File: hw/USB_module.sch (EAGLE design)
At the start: 34 parts, among them J1 GROVE-4P-2.0-3470130P1, J2 GROVE-4P-2.0-3470130P1, X1 22-23-2021, X2 47589-0001, X3 22-23-2021, X4 53047-04, X5 53047-04, X6 53047-06, X7 53047-06, X8 53047-06, X9 53047-04

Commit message: work in progress
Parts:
- U$6: value STM32F103CXTX -> STM32F303C; device st:STM32F103CXTX -> st:STM32F303C
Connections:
- removed net N$5: X7-5.S, X7-6.S
- removed net N$6: X8-5.S, X8-6.S
- net OSC_IN: now also U$6.PF0/OSC_IN; no longer U$6.PD0/OSC_IN
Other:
- moved on the sheet: X7-6, X8-6
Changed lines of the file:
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@@
 <part name="J1" library="OPL Eagle Library" deviceset="GROVE-4P-2.0" device="-3470130P1"/>
 <part name="+3V7" library="supply1" deviceset="+3V3" device=""/>
-<part name="U$6" library="st" deviceset="STM32F103CX" device="TX"/>
+<part name="U$6" library="st" deviceset="STM32F303C" device=""/>
 <part name="FRAME1" library="frames" deviceset="DINA3_L" device=""/>
 <part name="GND13" library="supply" deviceset="GND" device=""/>
@@
 <instance part="X7" gate="-4" x="254" y="139.7"/>
 <instance part="X7" gate="-5" x="254" y="137.16"/>
-<instance part="X7" gate="-6" x="254" y="137.16"/>
+<instance part="X7" gate="-6" x="254" y="134.62"/>
 <instance part="X8" gate="-1" x="254" y="124.46"/>
 <instance part="X8" gate="-2" x="254" y="121.92"/>
@@
 <instance part="X8" gate="-4" x="254" y="116.84"/>
 <instance part="X8" gate="-5" x="254" y="114.3"/>
-<instance part="X8" gate="-6" x="254" y="114.3"/>
+<instance part="X8" gate="-6" x="254" y="111.76"/>
 <instance part="X9" gate="-1" x="322.58" y="220.98"/>
 <instance part="X9" gate="-2" x="322.58" y="218.44"/>
@@
 <wire x1="50.8" y1="236.22" x2="50.8" y2="238.76" width="0.1524" layer="91"/>
 <label x="50.8" y="238.76" size="1.778" layer="95" rot="R90"/>
-<pinref part="U$6" gate="G$1" pin="PD0/OSC_IN"/>
+<pinref part="U$6" gate="G$1" pin="PF0/OSC_IN"/>
 </segment>
 <segment>
@@
 </segment>
 </net>
-<net name="N$5" class="0">
-<segment>
-<pinref part="X7" gate="-5" pin="S"/>
-<pinref part="X7" gate="-6" pin="S"/>
-</segment>
-</net>
-<net name="N$6" class="0">
-<segment>
-<pinref part="X8" gate="-5" pin="S"/>
-<pinref part="X8" gate="-6" pin="S"/>
-</segment>
-</net>

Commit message: layout of power oring section ongoing
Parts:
- added C10: (no value), rcl:C-EUC0805
- added C11: 10nF, rcl:C-EUC0603
- added D3: (no value), diode:DIODE-DO-214AC
- added D4: (no value), diode:DIODE-SOD123
- added D5, D6: (no value), dp_devices:ZENERSOD-323F
- added Q1: (no value), transistor-power:N-MOSFET-SO8S
- added R2: 100k, rcl:R-EU_R0603
- added R4: 4k7, rcl:R-EU_R0603
- added R5: (no value), rcl:R-EU_R0603
- added R6: 10k, rcl:R-EU_R0603
- added R7: 1k, rcl:R-EU_R0603
- added TVSD1, TVSD3: SMAJ24A, TVSD:TVSDSMA
- added U$7: LM5050-1, texas-instruments:LM5050-1
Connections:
- removed net USB_ID: X2.4
- new net N$10: C11.1, R5.1, U$7.VS
- new net N$5: R2.2, X2.4
- new net N$6: D5.C, R4.1, U$7.OFF
- new net N$9: Q1.G, U$7.GATE
- new net VBATT: C10.2, Q1.S, R6.2, TVSD1.K, U$7.VIN, X1-1.S
- new net VPSU: D3.A, R4.2, TVSD3.K, X3-1.S
- new net VSENSE: D6.C, R6.1, R7.2
- net GND: now also C10.1, C11.2, D5.A, D6.A, R2.1, R7.1, TVSD1.A, TVSD3.A, U$7.GND, X1-2.S, X3-2.S
- net USB_VBUS: now also D4.A
- net VIN: now also D3.C, D4.C, Q1.D, R5.2, U$7.OUT
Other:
- note added: "BATTERY VOLTAGE"
- note added: "POWER ORING"
- moved on the sheet: R11, R14

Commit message: layout almost finished
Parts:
- removed D3: (no value), diode:DIODE-DO-214AC
- removed D4: (no value), diode:DIODE-SOD123
- removed D5: (no value), dp_devices:ZENERSOD-323F
- removed TVSD3: SMAJ24A, TVSD:TVSDSMA
- removed X3: 22-23-2021, con-molex:22-23-2021
- removed X7, X8: 53047-06, con-molex:53047-06
- removed X9: 53047-04, con-molex:53047-04
- added C12: (no value), rcl:CPOL-EUE3.5-8
- added D1: MBR0520LT, diode:MBR0520LT
- added D2: (no value), dp_devices:ZENERSOD-323F
- added R8: 22, rcl:R-EU_R0603
- D6: value (none) -> 3V
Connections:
- removed net USB_DM: R11.1
- removed net USB_DP: R14.1
- removed net VPSU: D3.A, R4.2, TVSD3.K, X3-1.S
- new net !CS: U$6.PB12, X6-3.S
- new net MISO: U$6.PB14, X6-5.S
- new net MOSI: U$6.PB15, X6-6.S
- new net SCK: U$6.PB13, X6-4.S
- new net SCL: U$6.PA9, X4-3.S
- new net SDA: U$6.PA10, X4-4.S
- new net UART_RX: U$6.PB11, X5-4.S
- new net UART_TX: U$6.PB10, X5-3.S
- new net USB_N: R11.1, U$6.PA11
- new net USB_P: R14.1, U$6.PA12
- net +3V3: now also R8.1, X4-1.S, X5-1.S, X6-1.S
- net GND: now also C12.-, D2.A, X4-2.S, X5-2.S, X6-2.S; no longer D5.A, TVSD3.A, X3-2.S
- net N$32: now also R8.2
- net N$6: now also D2.C; no longer D5.C
- net USB_VBUS: now also D1.A, R4.2; no longer D4.A
- net VBATT: no longer R6.2
- net VIN: now also C12.+, D1.C, R6.2; no longer D3.C, D4.C
- net VSENSE: now also U$6.PB2-BOOT1
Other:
- moved on the sheet: C10, C11, Q1, R4, R5, TVSD1

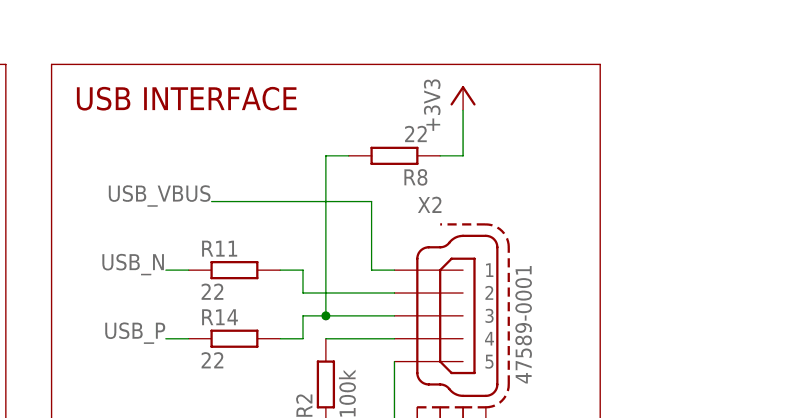
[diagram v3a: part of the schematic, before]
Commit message: updated USB R value
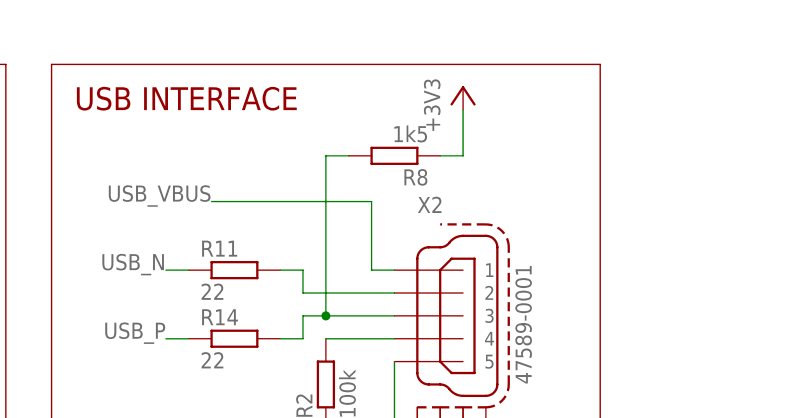
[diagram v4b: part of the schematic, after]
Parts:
- R8: value 22 -> 1k5
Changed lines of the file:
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@@
 <part name="GND41" library="supply" deviceset="GND" device=""/>
 <part name="GND24" library="supply1" deviceset="GND" device=""/>
-<part name="R8" library="rcl" deviceset="R-EU_" device="R0603" value="22"/>
+<part name="R8" library="rcl" deviceset="R-EU_" device="R0603" value="1k5"/>
 <part name="+3V8" library="supply1" deviceset="+3V3" device=""/>
 <part name="+3V9" library="supply1" deviceset="+3V3" device=""/>

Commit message: layout complete
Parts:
- removed D2: (no value), dp_devices:ZENERSOD-323F
- removed D6: 3V, dp_devices:ZENERSOD-323F
- removed Q1: (no value), transistor-power:N-MOSFET-SO8S
- removed R7: 1k, rcl:R-EU_R0603
- removed TVSD1: SMAJ24A, TVSD:TVSDSMA
- removed U$7: LM5050-1, texas-instruments:LM5050-1
- removed X1: 22-23-2021, con-molex:22-23-2021
- removed X2: 47589-0001, molex:47589-0001
- removed X4: 53047-04, con-molex:53047-04
- removed X6: 53047-06, con-molex:53047-06
- added J3: (no value), OPL-Connector:MICRO-SD-CARD-HOLDER-9P'MICROSD-9P'
- added J4: MICRO-USB-5P-340015001, OPL Eagle Library:MICRO-USB-5P-340015001
- added LED2: (no value), led:LEDCHIPLED_0805
- added R9: 100k, rcl:R-EU_R0603
- C10: value (none) -> 100n; device rcl:C-EUC0805 -> rcl:C-EUC0603
- C11: value 10nF -> 4.7u; device rcl:C-EUC0603 -> rcl:C-EUC0805
- C12: device rcl:CPOL-EUE3.5-8 -> rcl:CPOL-EUB/3528-21R
- R4: value 4k7 -> 100k
- R5: value (none) -> 100k
- R6: value 10k -> 330
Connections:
- removed net !CS: U$6.PB12, X6-3.S
- removed net MISO: U$6.PB14, X6-5.S
- removed net MOSI: U$6.PB15, X6-6.S
- removed net N$10: C11.1, R5.1, U$7.VS
- removed net N$9: Q1.G, U$7.GATE
- removed net SCK: U$6.PB13, X6-4.S
- removed net SCL: U$6.PA9, X4-3.S
- removed net SDA: U$6.PA10, X4-4.S
- removed net VBATT: C10.2, Q1.S, TVSD1.K, U$7.VIN, X1-1.S
- new net SD_!CD: J3.CDN, U$6.PA4
- new net SD_!CS: J3.CS, R9.1, U$6.PB12
- new net SD_CLK: J3.SCLK, U$6.PB13
- new net SD_LED: R6.2, U$6.PA3
- new net SD_MISO: J3.DO, R4.1, U$6.PB14
- new net SD_MOSI: J3.DI, R5.1, U$6.PB15
- net +3V3: now also C10.1, C11.1, J3.VDD, R4.2, R5.2, R9.2; no longer X4-1.S, X6-1.S
- net GND: now also C10.2, J3.VSS, J4.GND@1, J4.GND@2, J4.GND@3, LED2.A; no longer C10.1, D2.A, D6.A, R7.1, TVSD1.A, U$7.GND, X1-2.S, X2.5, X2.SHLD1, X2.SHLD2, X2.SHLD3, X2.SHLD4, X4-2.S, X6-2.S
- net N$3: now also J4.DM; no longer X2.2
- net N$32: now also J4.DP; no longer X2.3
- net N$5: now also J4.ID; no longer X2.4
- net N$6: now also LED2.C, R6.1; no longer D2.C, R4.1, U$7.OFF
- net USB_VBUS: now also J4.VCC; no longer R4.2, X2.1
- net VIN: no longer Q1.D, R5.2, R6.2, U$7.OUT
- net VSENSE: no longer D6.C, R6.1, R7.2
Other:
- note removed: "BATTERY VOLTAGE"
- moved on the sheet: C10, C11, R4, R5, R6

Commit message: layout completed
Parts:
- R4, R5, R9: value 100k -> 47k
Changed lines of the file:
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@@
 <part name="GND20" library="supply" deviceset="GND" device=""/>
 <part name="J3" library="OPL-Connector" deviceset="MICRO-SD-CARD-HOLDER-9P" device="'MICROSD-9P'"/>
-<part name="R4" library="rcl" deviceset="R-EU_" device="R0603" value="100k"/>
-<part name="R5" library="rcl" deviceset="R-EU_" device="R0603" value="100k"/>
-<part name="R9" library="rcl" deviceset="R-EU_" device="R0603" value="100k"/>
+<part name="R4" library="rcl" deviceset="R-EU_" device="R0603" value="47k"/>
+<part name="R5" library="rcl" deviceset="R-EU_" device="R0603" value="47k"/>
+<part name="R9" library="rcl" deviceset="R-EU_" device="R0603" value="47k"/>
 <part name="J4" library="OPL Eagle Library" deviceset="MICRO-USB-5P" device="-340015001"/>
 <part name="+3V9" library="supply1" deviceset="+3V3" device=""/>
